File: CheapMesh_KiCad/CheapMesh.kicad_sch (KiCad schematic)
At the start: 24 parts, among them J1 Conn_01x02_Pin, J2 Conn_01x09_Pin, J3 USB_A, J4 USB_C, J5 Conn_Coaxial, Q1 UMH3N, U1 L78L33, U2 HT-CT62, U3 AP2112K-3.3

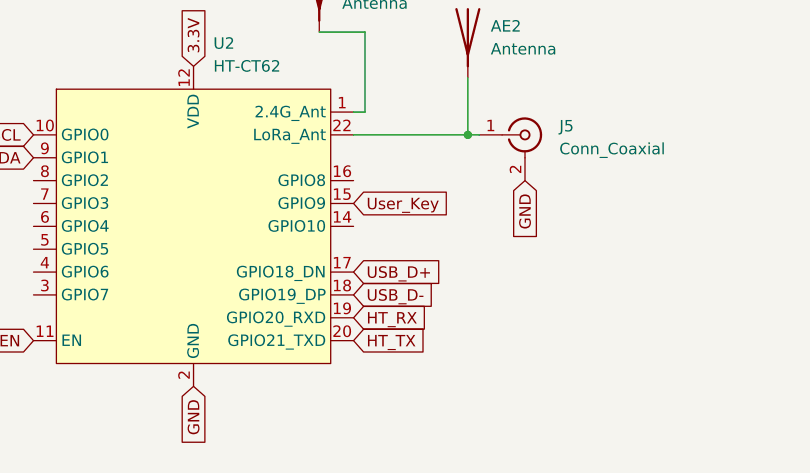
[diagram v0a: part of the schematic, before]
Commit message: invert USB_D+ USB_D- in schematics
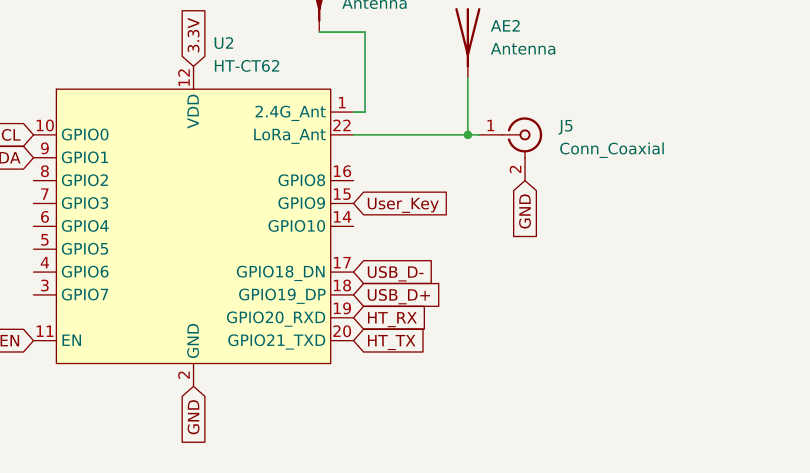
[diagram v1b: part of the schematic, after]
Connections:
- net USB_D+: now also U2.18 (GPIO19_DP); no longer U2.17 (GPIO18_DN)
- net USB_D-: now also U2.17 (GPIO18_DN); no longer U2.18 (GPIO19_DP)
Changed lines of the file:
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@@
 		)
 	)
-	(global_label "USB_D-"
+	(global_label "USB_D+"
 		(shape input)
 		(at 120.65 118.11 0)
@@
 		)
 	)
-	(global_label "USB_D+"
+	(global_label "USB_D-"
 		(shape input)
 		(at 120.65 115.57 0)
